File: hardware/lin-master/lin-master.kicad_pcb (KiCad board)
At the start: 2 copper layers, 46.2 x 28.4 mm, 15 parts, among them J1 QWIIC Connector, J2 Screw_Terminal_01x03, U1 Arduino_Nano_v3.x, U2 TJA1021T

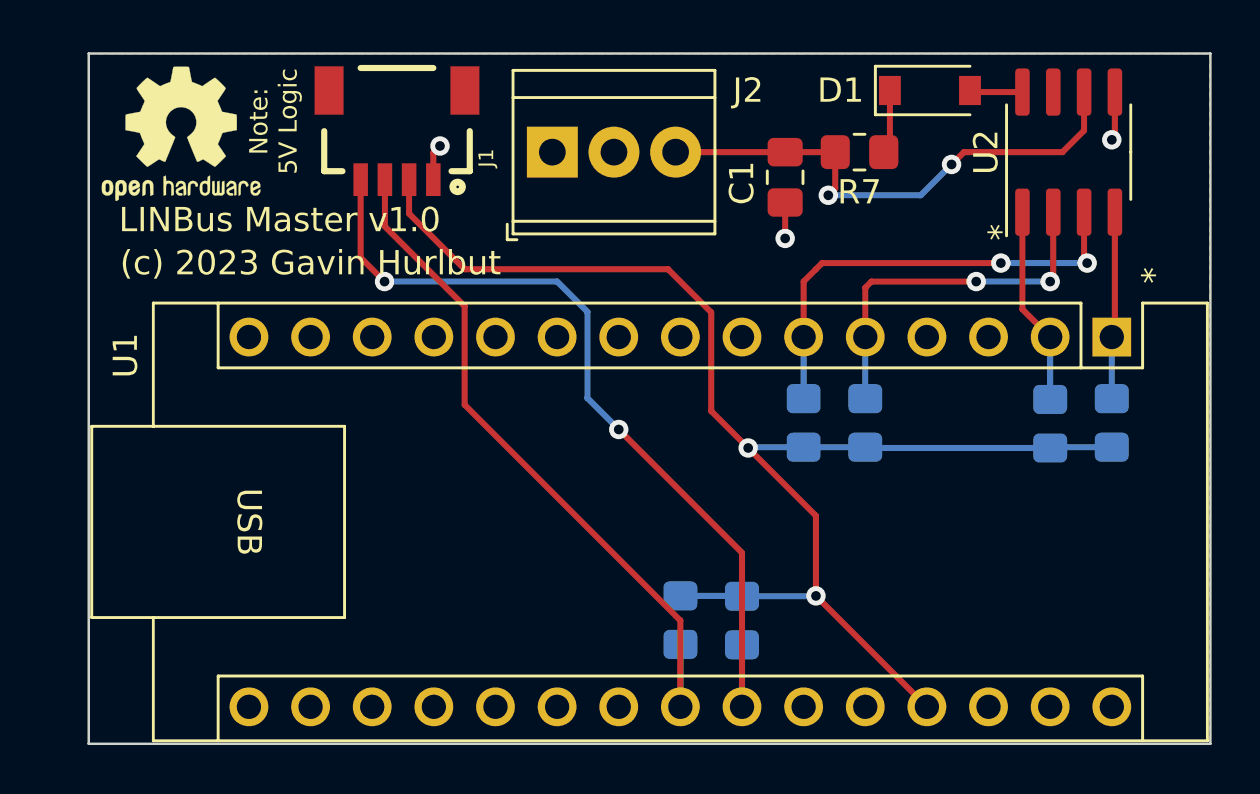
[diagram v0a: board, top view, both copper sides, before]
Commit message: Added I2C Addr lines and level translation
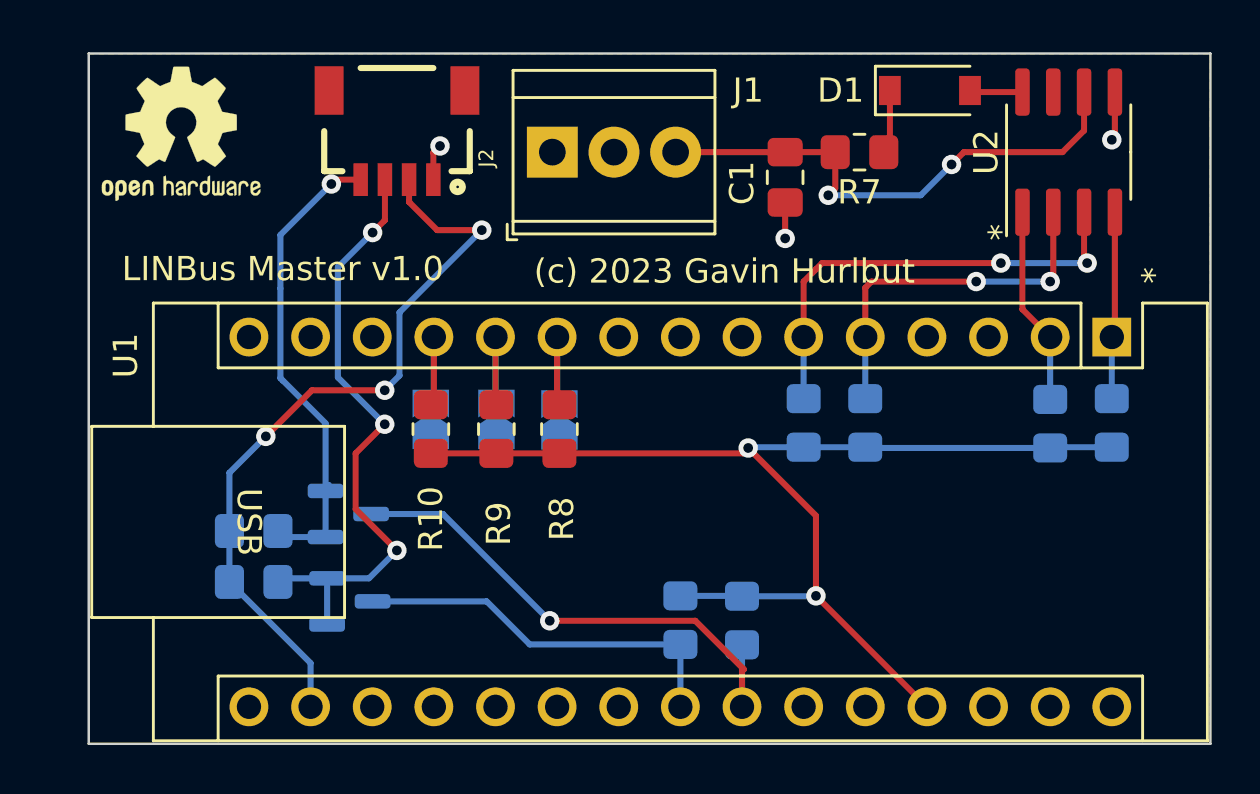
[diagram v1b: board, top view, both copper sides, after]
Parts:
- added JP1: Solder Jumper, Jumper:SolderJumper-2_P1.3mm_Open_TrianglePad1.0x1.5mm, B.Cu at (121.0, 89.5)
- added JP2: Solder Jumper, Jumper:SolderJumper-2_P1.3mm_Open_TrianglePad1.0x1.5mm, B.Cu at (118.4, 89.5)
- added JP3: Solder Jumper, Jumper:SolderJumper-2_P1.3mm_Open_TrianglePad1.0x1.5mm, B.Cu at (115.7, 89.5)
- added Q1: 2N7002, Package_TO_SOT_SMD:SOT-23, B.Cu at (112.3, 93.4)
- added Q2: 2N7002, Package_TO_SOT_SMD:SOT-23, B.Cu at (112.4, 97.0)
- added R10: 10k, Resistor_SMD:R_0805_2012Metric_Pad1.20x1.40mm_HandSolder, F.Cu at (115.7, 89.9)
- added R11: 10k, Resistor_SMD:R_0805_2012Metric_Pad1.20x1.40mm_HandSolder, B.Cu at (108.4, 96.2)
- added R12: 10k, Resistor_SMD:R_0805_2012Metric_Pad1.20x1.40mm_HandSolder, B.Cu at (108.4, 94.1)
- added R8: 10k, Resistor_SMD:R_0805_2012Metric_Pad1.20x1.40mm_HandSolder, F.Cu at (121.0, 89.9)
- added R9: 10k, Resistor_SMD:R_0805_2012Metric_Pad1.20x1.40mm_HandSolder, F.Cu at (118.4, 89.9)
- moved G*** 19.4 mm to (139.7, 94.9)
- renumbered J2 to J1, J1 to J2
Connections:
- J2 pad 2: +5V -> +3V3
- J2 pad 3: SDA5 -> SDA3V
- J2 pad 4: SCL5 -> SCL3V
- R5 pad 2: SDA5 -> SDA5V
- R6 pad 2: SCL5 -> SCL5V
- U1 pad 10: unconnected-(U1-Pad10) -> A0
- U1 pad 11: unconnected-(U1-Pad11) -> A1
- U1 pad 12: unconnected-(U1-Pad12) -> A2
- U1 pad 23: SDA5 -> SDA5V
- U1 pad 24: SCL5 -> SCL5V
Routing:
- net SCL5: track 35.0 -> 0.00 mm, vias 2 -> 0
- net +3V3: track 0.00 -> 31.4 mm, vias 0 -> 3
- net SDA5: track 29.3 -> 0.00 mm
- net SDA3V: track 0.00 -> 25.4 mm, vias 0 -> 3
- net SCL5V: track 0.00 -> 22.1 mm, vias 0 -> 1
- net SCL3V: track 0.00 -> 19.8 mm, vias 0 -> 1
- net SDA5V: track 0.00 -> 16.0 mm
- net +5V: track 56.1 -> 47.5 mm
- net A0: track 0.00 -> 5.57 mm
- net A2: track 0.00 -> 5.57 mm
- net A1: track 0.00 -> 5.49 mm
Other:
- board text removed: "Note: 5V Logic"

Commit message: Added firmware for lin-master
- also added I2C address selection, and built-in 3.3V->5V translation
  and a second QWIIC connector.
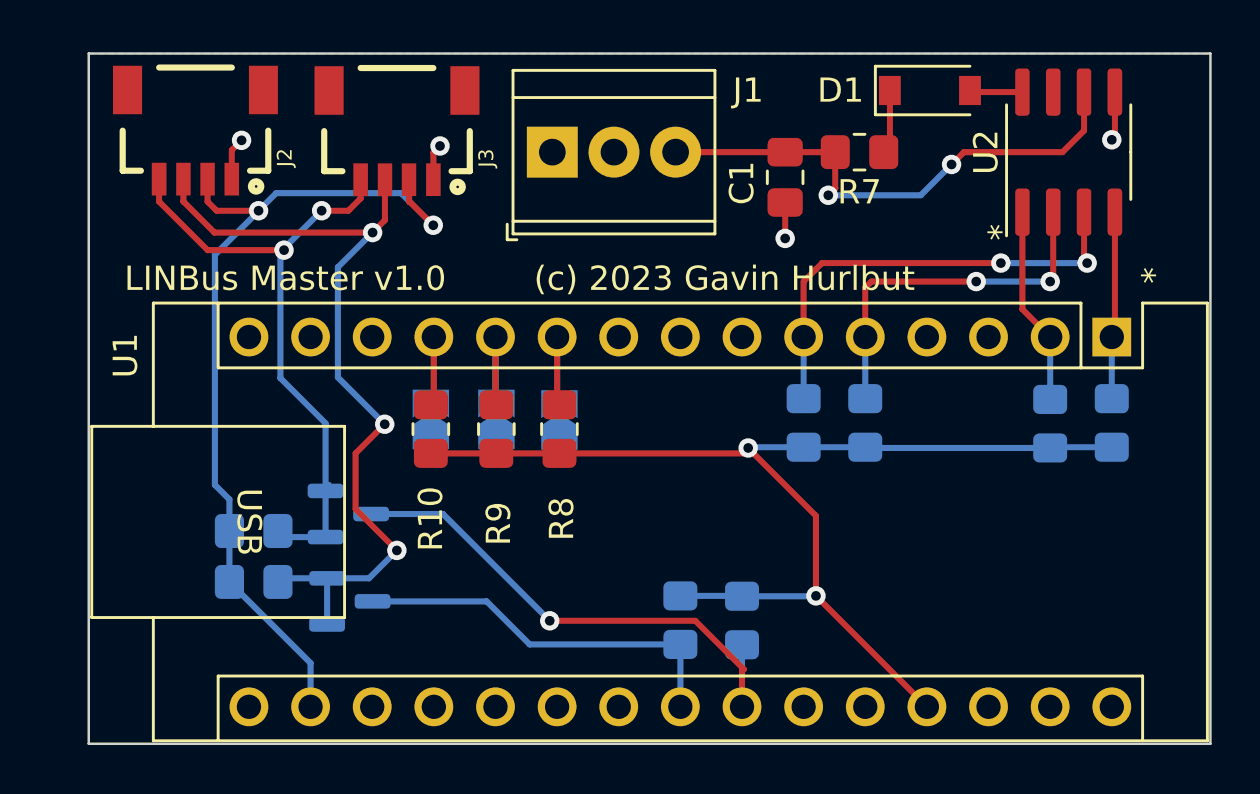
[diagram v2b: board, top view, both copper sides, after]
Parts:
- added J2: QWIIC Connector, SparkFun-Connectors:1X04_1MM_RA, F.Cu at (106.0, 79.6)
- REF**: moved to B.Cu
- moved REF** 25.1 mm to (125.5, 92.7), turned to 180 degrees
- renumbered J2 to J3
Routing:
- net SDA3V: track 25.4 -> 34.7 mm
- net SCL3V: track 19.8 -> 26.8 mm, vias 1 -> 2
- net +3V3: track 31.4 -> 37.3 mm, vias 3 -> 2
- net GND: track 5.00 -> 6.77 mm, vias 3 -> 4
